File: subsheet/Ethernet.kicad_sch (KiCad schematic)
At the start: 6 parts, among them J1301 Conn_01x06, J1302 Conn_01x06

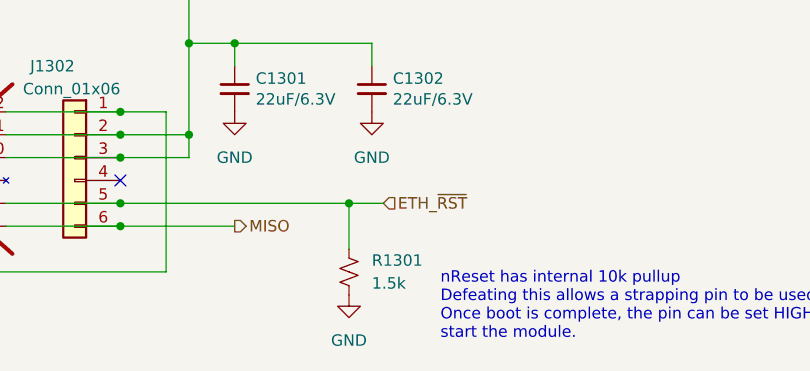
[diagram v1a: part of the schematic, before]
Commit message: Add order codes for all components
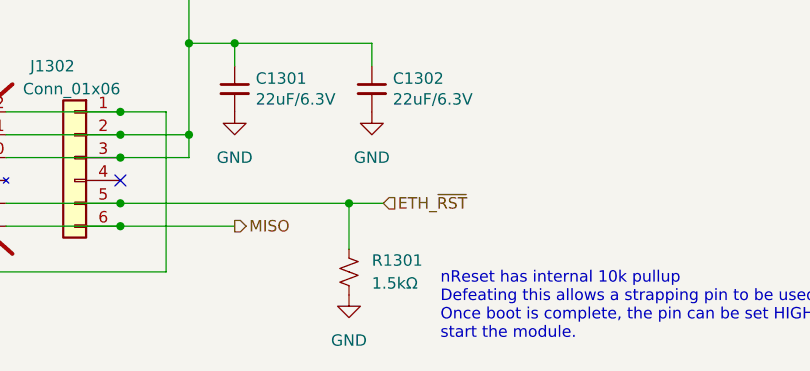
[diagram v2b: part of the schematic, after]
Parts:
- R1301: value 1.5k -> 1.5kΩ
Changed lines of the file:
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@@
+			)
+		)
+		(property "I2C address" ""
+			(at 187.96 78.74 0)
+			(effects
+				(font
+					(size 1.27 1.27)
+				)
+				(hide yes)
 			)
 		)
@@
 			)
 		)
+		(property "I2C address" ""
+			(at 137.16 87.63 0)
+			(effects
+				(font
+					(size 1.27 1.27)
+				)
+				(hide yes)
+			)
+		)
 		(pin "1"
 		)
@@
 			)
 		)
+		(property "I2C address" ""
+			(at 121.92 86.36 0)
+			(effects
+				(font
+					(size 1.27 1.27)
+				)
+				(hide yes)
+			)
+		)
 		(pin "1"
 		)
@@
 		)
 		(property "JLCPCB_CORRECTION" "0;6.35;90"
+			(at 154.94 86.36 0)
+			(effects
+				(font
+					(size 1.27 1.27)
+				)
+				(hide yes)
+			)
+		)
+		(property "I2C address" ""
 			(at 154.94 86.36 0)
 			(effects
@@
 			)
 		)
-		(property "Value" "1.5k"
+		(property "Value" "1.5kΩ"
 			(at 187.96 100.3299 0)
 			(effects
@@
 		(property "LCSC" "C22843 "
 			(at 185.42 99.06 90)
+			(effects
+				(font
+					(size 1.27 1.27)
+				)
+				(hide yes)
+			)
+		)
+		(property "I2C address" ""
+			(at 185.42 99.06 0)
 			(effects
 				(font
@@
 			(at 172.72 78.74 0)
 			(effects
+				(font
+					(size 1.27 1.27)
+				)
+				(hide yes)
+			)
+		)
+		(property "I2C address" ""
+			(at 172.72 78.74 0)
+			(effects

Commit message: Add JLCPCB corrections for new components
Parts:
- J1301, J1302: JLCPCB_IGNORE (none) -> 1
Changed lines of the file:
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@@
+			)
+		)
+		(property "JLCPCB_IGNORE" "1"
+			(at 121.92 86.36 0)
+			(effects
+				(font
+					(size 1.27 1.27)
+				)
+				(hide yes)
 			)
 		)
@@
 			(at 154.94 86.36 0)
 			(effects
+				(font
+					(size 1.27 1.27)
+				)
+				(hide yes)
+			)
+		)
+		(property "JLCPCB_IGNORE" "1"
+			(at 154.94 86.36 0)
+			(effects

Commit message: Silkscreen work. Edit tittle block/version number
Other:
- company: copyright Escape This 2024 -> (c) Vincent Dalstra
- title: Puzzle Board -> Untitled 4-layer JLCPCB
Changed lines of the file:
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@@
 	(paper "A4")
 	(title_block
-		(title "Puzzle Board")
-		(date "2024-03-20")
-		(rev "4.0.0")
-		(company "copyright Escape This 2024")
+		(title "Untitled 4-layer JLCPCB")
+		(date "2024-06-14")
+		(rev "1.0.0")
+		(company "(c) Vincent Dalstra")
 		(comment 1 "Drawn by: VGD")
 		(comment 2 "Check by:")

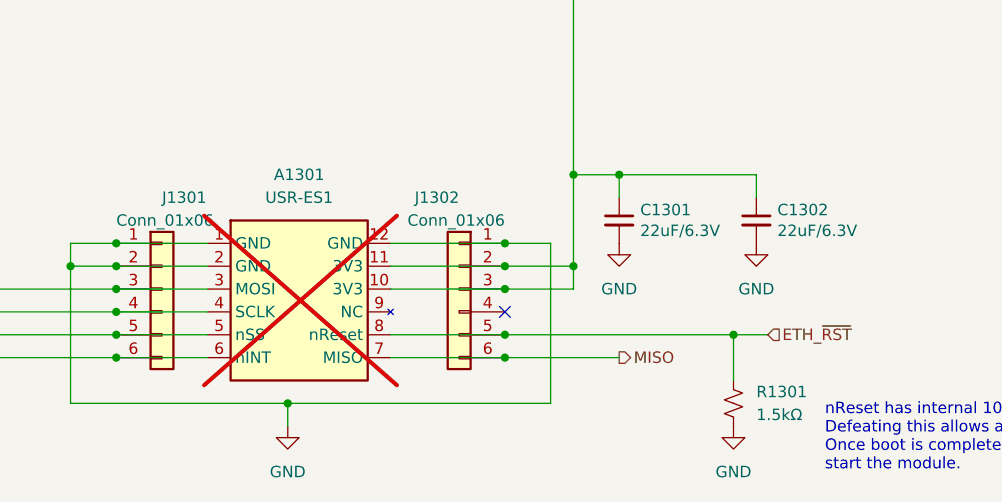
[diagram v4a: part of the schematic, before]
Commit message: Move all subsheets into 'main' subsheet, below root
Keeping all the subsheets in a dedicated 'subsheet' folder makes things
much, much neater. However, specifying filepaths for subsheets has an
interesting problem; they use paths RELATIVE TO THE PARENT SHEET.

The consequence of is that if a subsheet is part of the root sheet, it
needs to be prefixed with 'subsheet/', but NOT if it's further down.
This inconsistency can be resolved by having a single 'main' sheet at
the top that doesn't move.

It's also useful to have a top-level space to put down changelogs,
descriptions etc.
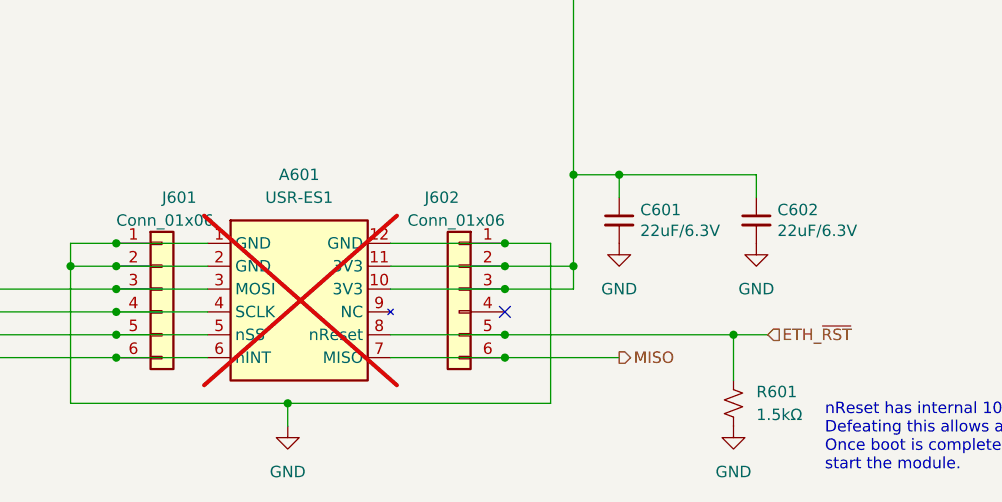
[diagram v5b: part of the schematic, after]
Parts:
- renumbered A1301 to A601, C1301 to C601, C1302 to C602, J1301 to J601, J1302 to J602, R1301 to R601
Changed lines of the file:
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@@
 		(shape input)
 		(at 99.06 86.36 180)
-		(fields_autoplaced yes)
 		(effects
 			(font
@@
 		(shape input)
 		(at 99.06 91.44 180)
-		(fields_autoplaced yes)
 		(effects
 			(font
@@
 		(shape output)
 		(at 172.72 93.98 0)
-		(fields_autoplaced yes)
 		(effects
 			(font
@@
 		(shape input)
 		(at 189.23 91.44 0)
-		(fields_autoplaced yes)
 		(effects
 			(font
@@
 		(shape input)
 		(at 99.06 93.98 180)
-		(fields_autoplaced yes)
 		(effects
 			(font
@@
 		(shape input)
 		(at 99.06 88.9 180)
-		(fields_autoplaced yes)
 		(effects
 			(font
@@
 		(dnp no)
 		(fields_autoplaced yes)
-		(property "Reference" "#PWR01302"
+		(property "Reference" "#PWR602"
 			(at 142.24 34.29 0)
 			(effects
@@
 		(instances
 			(project "ESP_bare_chip_test_board"
-				(path "/45b6f84a-e69b-48be-a49b-bc68872e2c15/55308f0d-6d1f-4d67-a924-a225ca5de0ad"
-					(reference "#PWR01302")
+				(path "/45b6f84a-e69b-48be-a49b-bc68872e2c15/f48098a1-cacc-4192-b650-2a34a2ba76dc/f947886a-5d04-4d2b-83fd-e23ae6b83691"
+					(reference "#PWR602")
 					(unit 1)
 				)
@@
 		(on_board yes)
 		(dnp no)
-		(property "Reference" "C1302"
+		(property "Reference" "C602"
 			(at 190.2968 77.5716 0)
 			(effects
@@
 		(instances
 			(project "ESP_bare_chip_test_board"
-				(path "/45b6f84a-e69b-48be-a49b-bc68872e2c15/55308f0d-6d1f-4d67-a924-a225ca5de0ad"
-					(reference "C1302")
+				(path "/45b6f84a-e69b-48be-a49b-bc68872e2c15/f48098a1-cacc-4192-b650-2a34a2ba76dc/f947886a-5d04-4d2b-83fd-e23ae6b83691"
+					(reference "C602")
 					(unit 1)
 				)
@@
 		(dnp no)
 		(fields_autoplaced yes)
-		(property "Reference" "#PWR01303"
+		(property "Reference" "#PWR603"
 			(at 172.72 87.63 0)
 			(effects
@@
 		(instances
 			(project "ESP_bare_chip_test_board"
-				(path "/45b6f84a-e69b-48be-a49b-bc68872e2c15/55308f0d-6d1f-4d67-a924-a225ca5de0ad"
-					(reference "#PWR01303")
+				(path "/45b6f84a-e69b-48be-a49b-bc68872e2c15/f48098a1-cacc-4192-b650-2a34a2ba76dc/f947886a-5d04-4d2b-83fd-e23ae6b83691"
+					(reference "#PWR603")
 					(unit 1)
 				)
@@
 		(dnp yes)
 		(fields_autoplaced yes)
-		(property "Reference" "A1301"
+		(property "Reference" "A601"
 			(at 137.16 73.66 0)
 			(effects
@@
 		(instances
 			(project "ESP_bare_chip_test_board"
-				(path "/45b6f84a-e69b-48be-a49b-bc68872e2c15/55308f0d-6d1f-4d67-a924-a225ca5de0ad"
-					(reference "A1301")
+				(path "/45b6f84a-e69b-48be-a49b-bc68872e2c15/f48098a1-cacc-4192-b650-2a34a2ba76dc/f947886a-5d04-4d2b-83fd-e23ae6b83691"
+					(reference "A601")
 					(unit 1)
 				)
@@
 		(dnp no)
 		(fields_autoplaced yes)
-		(property "Reference" "#PWR01305"
+		(property "Reference" "#PWR605"
 			(at 187.96 87.63 0)
 			(effects
@@
 		(instances
 			(project "ESP_bare_chip_test_board"
-				(path "/45b6f84a-e69b-48be-a49b-bc68872e2c15/55308f0d-6d1f-4d67-a924-a225ca5de0ad"
-					(reference "#PWR01305")
+				(path "/45b6f84a-e69b-48be-a49b-bc68872e2c15/f48098a1-cacc-4192-b650-2a34a2ba76dc/f947886a-5d04-4d2b-83fd-e23ae6b83691"
+					(reference "#PWR605")
 					(unit 1)
 				)
@@
 		(dnp no)
 		(fields_autoplaced yes)
-		(property "Reference" "#PWR01304"
+		(property "Reference" "#PWR604"
 			(at 185.42 107.95 0)
 			(effects
@@
 		(instances
 			(project "ESP_bare_chip_test_board"
-				(path "/45b6f84a-e69b-48be-a49b-bc68872e2c15/55308f0d-6d1f-4d67-a924-a225ca5de0ad"
-					(reference "#PWR01304")
+				(path "/45b6f84a-e69b-48be-a49b-bc68872e2c15/f48098a1-cacc-4192-b650-2a34a2ba76dc/f947886a-5d04-4d2b-83fd-e23ae6b83691"
+					(reference "#PWR604")
 					(unit 1)
 				)
@@
 		(on_board yes)
 		(dnp no)
-		(property "Reference" "J1301"
+		(property "Reference" "J601"
 			(at 121.92 76.2 0)
 			(effects
@@
 		(instances
 			(project "ESP_bare_chip_test_board"
-				(path "/45b6f84a-e69b-48be-a49b-bc68872e2c15/55308f0d-6d1f-4d67-a924-a225ca5de0ad"
-					(reference "J1301")
+				(path "/45b6f84a-e69b-48be-a49b-bc68872e2c15/f48098a1-cacc-4192-b650-2a34a2ba76dc/f947886a-5d04-4d2b-83fd-e23ae6b83691"
+					(reference "J601")
 					(unit 1)
 				)
@@
 		(on_board yes)
 		(dnp no)
-		(property "Reference" "J1302"
+		(property "Reference" "J602"
 			(at 154.94 76.2 0)
 			(effects
@@
 		(instances
 			(project "ESP_bare_chip_test_board"
-				(path "/45b6f84a-e69b-48be-a49b-bc68872e2c15/55308f0d-6d1f-4d67-a924-a225ca5de0ad"
-					(reference "J1302")
+				(path "/45b6f84a-e69b-48be-a49b-bc68872e2c15/f48098a1-cacc-4192-b650-2a34a2ba76dc/f947886a-5d04-4d2b-83fd-e23ae6b83691"
+					(reference "J602")
 					(unit 1)
 				)
@@
 		(dnp no)
 		(fields_autoplaced yes)
-		(property "Reference" "R1301"
+		(property "Reference" "R601"
 			(at 187.96 97.7899 0)
 			(effects
@@
 		(instances
 			(project "ESP_bare_chip_test_board"
-				(path "/45b6f84a-e69b-48be-a49b-bc68872e2c15/55308f0d-6d1f-4d67-a924-a225ca5de0ad"
-					(reference "R1301")
+				(path "/45b6f84a-e69b-48be-a49b-bc68872e2c15/f48098a1-cacc-4192-b650-2a34a2ba76dc/f947886a-5d04-4d2b-83fd-e23ae6b83691"
+					(reference "R601")
 					(unit 1)
 				)
@@
 		(on_board yes)
 		(dnp no)
-		(property "Reference" "C1301"
+		(property "Reference" "C601"
 			(at 175.0568 77.5716 0)
 			(effects
@@
 		(instances
 			(project "ESP_bare_chip_test_board"
-				(path "/45b6f84a-e69b-48be-a49b-bc68872e2c15/55308f0d-6d1f-4d67-a924-a225ca5de0ad"
-					(reference "C1301")
+				(path "/45b6f84a-e69b-48be-a49b-bc68872e2c15/f48098a1-cacc-4192-b650-2a34a2ba76dc/f947886a-5d04-4d2b-83fd-e23ae6b83691"
+					(reference "C601")
 					(unit 1)
 				)
@@
 		(dnp no)
 		(fields_autoplaced yes)
-		(property "Reference" "#PWR01301"
+		(property "Reference" "#PWR601"
 			(at 135.89 107.95 0)
 			(effects
@@
 		(instances
 			(project "ESP_bare_chip_test_board"
-				(path "/45b6f84a-e69b-48be-a49b-bc68872e2c15/55308f0d-6d1f-4d67-a924-a225ca5de0ad"
-					(reference "#PWR01301")
-					(unit 1)
-				)
+				(path "/45b6f84a-e69b-48be-a49b-bc68872e2c15/f48098a1-cacc-4192-b650-2a34a2ba76dc/f947886a-5d04-4d2b-83fd-e23ae6b83691"
+					(reference "#PWR601")
+					(unit 1)
+				)
